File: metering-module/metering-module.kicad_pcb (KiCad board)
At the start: 2 copper layers, 87 x 31 mm, 25 parts, among them J1 North, J2 South, Q1 MMBT3904, Q2 MMBT3904, U1 LTV-817S, U2 LTV-817S, U3 BA033CC0FP-E2, U4 MAX3486, U5 MAX3486

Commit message: Ongoing
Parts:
- added J3: West, Connector_PinHeader_2.54mm:PinHeader_1x14_P2.54mm_Vertical, F.Cu at (163.5, 83.2)
- added J4: East, Connector_PinHeader_2.54mm:PinHeader_1x14_P2.54mm_Vertical, F.Cu at (130.3, 108.0)
- added J5: RJ12, Connector_RJ:RJ12_Amphenol_54601, F.Cu at (117.4, 84.0)
- moved C1 7.65 mm to (136.2, 101.6)
- moved C2 7.65 mm to (141.0, 101.6)
- moved D1 7.65 mm to (131.2, 88.1)
- moved D2 7.65 mm to (131.2, 91.6)
- moved F1 7.65 mm to (131.2, 99.1)
- moved R5 7.65 mm to (131.2, 95.1)
- moved U3 7.65 mm to (138.6, 92.9)
- moved R1 3.90 mm to (156.9, 89.5)
- moved U1 3.60 mm to (164.9, 89.2)

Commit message: Ongoing Work
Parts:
- removed H1, H2: MountingHole_Pad, MountingHole:MountingHole_4.3mm_M4
- removed J5: RJ12, Connector_RJ:RJ12_Amphenol_54601
- added C5: 100nF, Capacitor_SMD:C_1206_3216Metric_Pad1.33x1.80mm_HandSolder, F.Cu at (147.0, 97.5)
- added C6: 100nF, Capacitor_SMD:C_1206_3216Metric_Pad1.33x1.80mm_HandSolder, F.Cu at (147.0, 89.5)
- added D5: D_TVS, Diode_SMD:D_0603_1608Metric_Pad1.05x0.95mm_HandSolder, F.Cu at (112.0, 87.5)
- added D6: D_TVS, Diode_SMD:D_0603_1608Metric_Pad1.05x0.95mm_HandSolder, F.Cu at (112.0, 84.0)
- added D7: D_TVS, Diode_SMD:D_0603_1608Metric_Pad1.05x0.95mm_HandSolder, F.Cu at (164.0, 103.0)
- added D8: D_TVS, Diode_SMD:D_0603_1608Metric_Pad1.05x0.95mm_HandSolder, F.Cu at (164.0, 107.5)
- added R10: R, Resistor_SMD:R_1206_3216Metric_Pad1.30x1.75mm_HandSolder, F.Cu at (169.0, 103.0)
- added R11: R, Resistor_SMD:R_1206_3216Metric_Pad1.30x1.75mm_HandSolder, F.Cu at (169.0, 107.5)
- added R6: R, Resistor_SMD:R_1206_3216Metric_Pad1.30x1.75mm_HandSolder, F.Cu at (118.0, 87.5)
- added R7: R, Resistor_SMD:R_1206_3216Metric_Pad1.30x1.75mm_HandSolder, F.Cu at (118.0, 84.0)
- added R8: R, Resistor_SMD:R_1206_3216Metric_Pad1.30x1.75mm_HandSolder, F.Cu at (150.5, 97.5)
- added R9: R, Resistor_SMD:R_1206_3216Metric_Pad1.30x1.75mm_HandSolder, F.Cu at (150.5, 89.5)
- added TP1: Shield, TestPoint:TestPoint_Pad_D4.0mm, B.Cu at (143.0, 95.5)
- C2: value C -> 100nF
- R5: value R -> 10k
- moved J4 29.2 mm to (159.5, 108.5), turned to 270 degrees
- moved D4 17.8 mm to (175.5, 101.5)
- moved R4 8.35 mm to (171.0, 97.5), turned to 270 degrees
- moved D3 8.30 mm to (175.5, 85.0)
- moved U5 6.80 mm to (115.0, 92.5)
- moved C1 5.73 mm to (130.5, 101.0)
- moved U3 5.69 mm to (133.0, 92.0)
- moved C2 5.53 mm to (135.5, 101.0)
- moved D1 5.23 mm to (126.0, 87.5)
- moved D2 5.23 mm to (126.0, 91.0)
- moved F1 5.23 mm to (126.0, 98.5)
- moved R5 5.23 mm to (126.0, 94.5)
- moved C3 4.74 mm to (115.0, 97.5), turned to 0 degrees
- moved C4 4.74 mm to (115.0, 107.5), turned to 0 degrees
- moved J3 4.06 mm to (159.5, 82.5)
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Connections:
- J1 pad 5: Net-(J1-Pad5) -> Relay_1
- J1 pad 6: Net-(J1-Pad6) -> Relay_0
- J1 pad 7: Net-(J1-Pad7) -> GND1
- J1 pad 8: Net-(J1-Pad8) -> VS
- J2 pad 1: Net-(J2-Pad1) -> VCC
- J2 pad 2: Net-(J2-Pad2) -> GND
- J2 pad 5: Net-(J2-Pad5) -> RS485_0_A
- J2 pad 6: Net-(J2-Pad6) -> RS485_0_B
- J2 pad 7: Net-(J2-Pad7) -> RS485_1_A
- J2 pad 8: Net-(J2-Pad8) -> RS485_1_B
- U4 pad 6: RS485_0_A -> RS485_1_A
- U4 pad 7: RS485_0_B -> RS485_1_B
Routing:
- net +3V3: track 3.00 -> 71.6 mm
- net S0_1: track 0.00 -> 47.6 mm
- net VS: track 0.00 -> 43.1 mm
- net VCC: track 0.00 -> 36.3 mm
- net S0_0: track 0.00 -> 36.3 mm
- net GND1: track 0.00 -> 23.2 mm
- net GNDPWR: track 0.00 -> 21.9 mm
- net RS485_0_B: track 0.00 -> 15.0 mm
- net RS485_1_B: track 0.00 -> 12.7 mm
- net RS485_0_A: track 0.00 -> 12.5 mm
- net Relay_1: track 0.00 -> 11.3 mm
- net Relay_0: track 0.00 -> 10.3 mm
- net RS485_1_A: track 0.00 -> 9.93 mm
- net Net-(R4-Pad2): track 0.00 -> 3.85 mm
- net Net-(R3-Pad2): track 0.00 -> 3.85 mm
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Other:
- board size 87 x 31 mm -> 86 x 31 mm
- board text added: "BOT"
- board text added: "TOP"

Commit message: Ongoing Work. Still not ready for small and dedicated commits.
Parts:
- removed D5, D6: D_TVS, Diode_SMD:D_0603_1608Metric_Pad1.05x0.95mm_HandSolder
- removed R6, R7: R, Resistor_SMD:R_1206_3216Metric_Pad1.30x1.75mm_HandSolder
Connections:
- net Net-(J4-Pad4) renamed U0TXD
- net Net-(J4-Pad5) renamed U0RXD
- J1 pad 1: Net-(J1-Pad1) -> GND
- J1 pad 2: Net-(J1-Pad2) -> S0_1
- J1 pad 3: Net-(J1-Pad3) -> GND
- J1 pad 4: Net-(J1-Pad4) -> S0_0
- J2 pad 2: GND -> VCC
- J2 pad 3: Net-(J2-Pad3) -> GND
- J2 pad 4: Net-(J2-Pad4) -> GNDPWR
- J3 pad 10: Net-(J3-Pad10) -> RS485_0_TX
- J3 pad 12: Net-(J3-Pad12) -> S0_1
- J3 pad 13: Net-(J3-Pad13) -> SW0
- J3 pad 4: Net-(J3-Pad4) -> RS485_0_RX
- J3 pad 5: Net-(J3-Pad5) -> S0_0
- J3 pad 6: Net-(J3-Pad6) -> RS485_1_RX
- J3 pad 9: Net-(J3-Pad9) -> RS485_0_TXE
- J4 pad 10: Net-(J4-Pad10) -> SW1
- J4 pad 12: Net-(J4-Pad12) -> RS485_1_TXE
- J4 pad 13: Net-(J4-Pad13) -> RS485_1_TX
- U4 pad 1: RS485_0_RX -> RS485_1_RX
- U4 pad 2: RS485_0_TXE -> RS485_1_TXE
- U4 pad 3: RS485_0_TXE -> RS485_1_TXE
- U4 pad 4: RS485_0_TX -> RS485_1_TX
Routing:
- net GNDPWR: track 21.9 -> 95.3 mm
- net RS485_0_RX: track 0.00 -> 40.4 mm, vias 0 -> 1
- net RS485_1_RX: track 0.00 -> 38.5 mm, vias 0 -> 2
- net RS485_1_TXE: track 0.00 -> 27.0 mm
- net RS485_0_TXE: track 2.54 -> 27.0 mm, vias 0 -> 1
- net RS485_0_TX: track 0.00 -> 22.5 mm, vias 0 -> 1
- net RS485_1_TX: track 0.00 -> 16.6 mm
- net +3V3: track 71.6 -> 56.7 mm, vias 0 -> 2
- net S0_1: track 47.6 -> 61.8 mm
- net S0_0: track 36.3 -> 50.1 mm
- net Net-(D6-Pad2): track 3.58 -> 0.00 mm
- net Net-(D5-Pad2): track 3.58 -> 0.00 mm
- net VCC: track 36.3 -> 34.7 mm, vias 0 -> 1

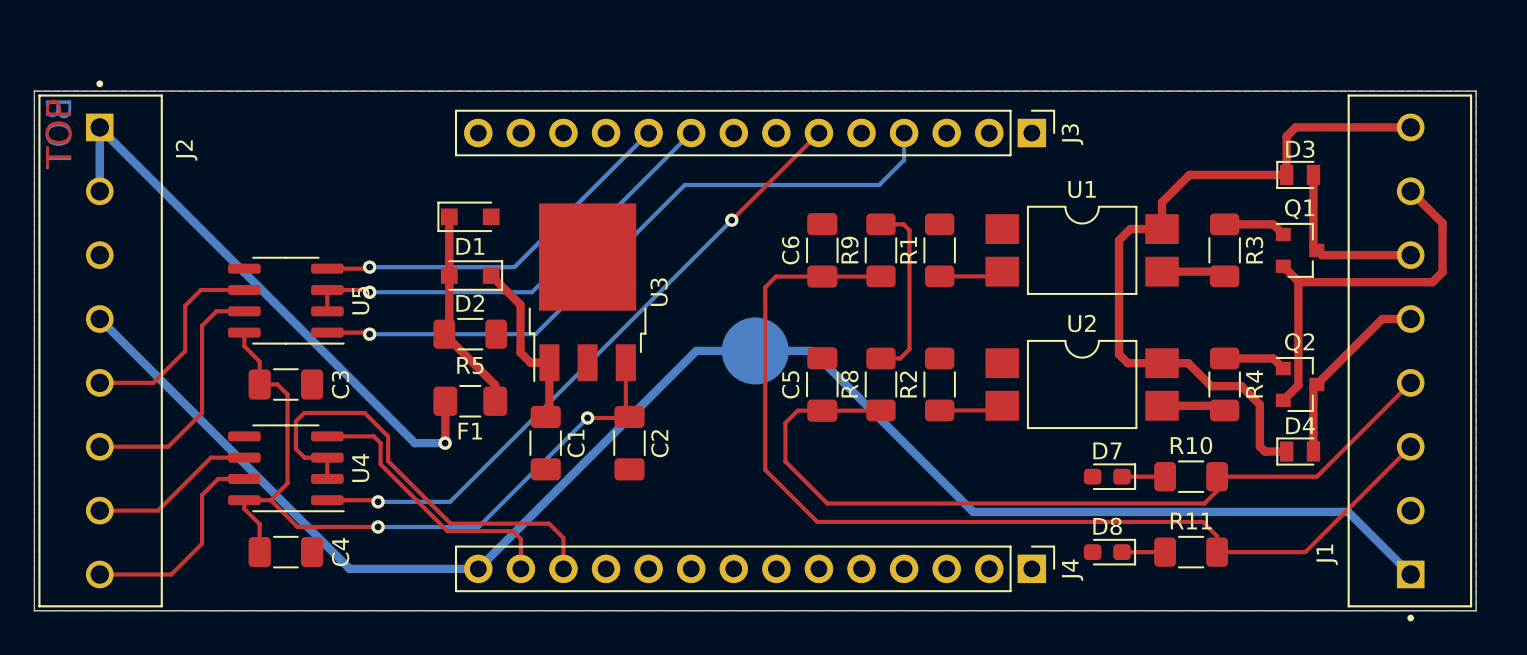
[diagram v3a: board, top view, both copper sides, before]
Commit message: Use a GPIO expander for metering module to safe pins
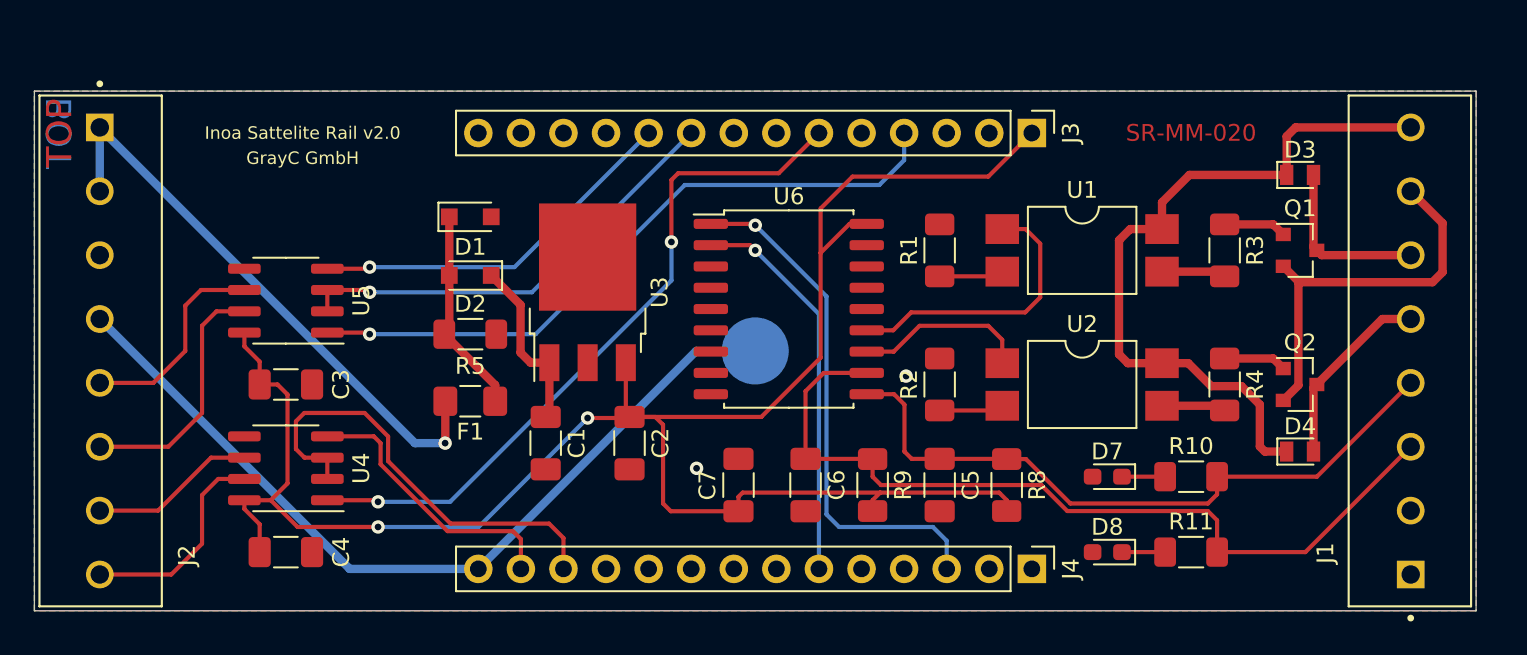
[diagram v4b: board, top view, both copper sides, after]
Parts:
- added C7: 100nF, Capacitor_SMD:C_1206_3216Metric_Pad1.33x1.80mm_HandSolder, F.Cu at (142.0, 103.5)
- added U6: MCP23008-xSO, Package_SO:SOIC-18W_7.5x11.6mm_P1.27mm, F.Cu at (145.0, 93.0)
- moved C6 14.0 mm to (146.0, 103.5), turned to 270 degrees
- moved R9 14.0 mm to (150.0, 103.5), turned to 270 degrees
- moved R8 9.60 mm to (158.0, 103.5), turned to 270 degrees
- moved C5 9.22 mm to (154.0, 103.5), turned to 270 degrees
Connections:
- net U0RXD renamed Net-(J4-Pad5)
- net U0TXD renamed Net-(J4-Pad4)
- J3 pad 12: S0_1 -> Net-(J3-Pad12)
- J3 pad 13: SW0 -> Net-(J3-Pad13)
- J3 pad 5: S0_0 -> Net-(J3-Pad5)
- J4 pad 10: SW1 -> Net-(J4-Pad10)
- J4 pad 3: Net-(J4-Pad3) -> I2C_SCL
- J4 pad 6: Net-(J4-Pad6) -> I2C_SDA
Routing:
- net +3V3: track 56.7 -> 115.8 mm
- net GNDPWR: track 95.3 -> 50.7 mm
- net I2C_SCL: track 0.00 -> 31.2 mm, vias 0 -> 1
- net I2C_SDA: track 0.00 -> 23.4 mm, vias 0 -> 1
- net SW0: track 0.00 -> 17.0 mm
- net S0_1: track 61.8 -> 50.9 mm
- net SW1: track 0.00 -> 10.5 mm
- net S0_0: track 50.1 -> 40.4 mm
- net RS485_1_RX: track 38.5 -> 42.0 mm
- net GND: vias 0 -> 2
- added copper zone on B.Cu, net GND
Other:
- board text added: "GrayC GmbH"
- board text added: "Inoa Sattelite Rail v2.0"
- board text added: "SR-MM-020"

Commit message: Introduce new serial numbering scheme
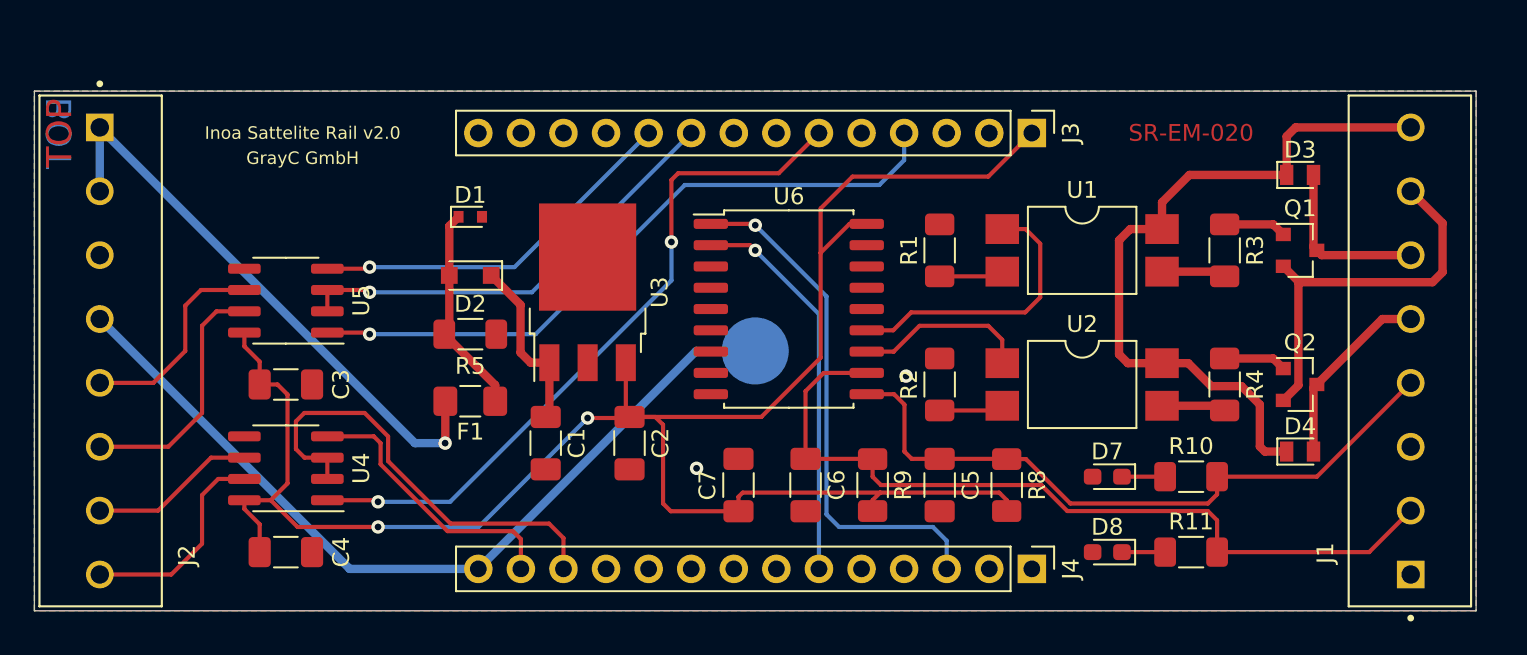
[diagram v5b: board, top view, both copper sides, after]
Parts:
- D1: value D_TVS -> 25V; footprint Diode_SMD:D_SOD-323_HandSoldering -> Diode_SMD:D_SOD-523
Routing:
- net S0_1: track 50.9 -> 49.3 mm
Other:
- board text added: "SR-EM-020"
- board text removed: "SR-MM-020"
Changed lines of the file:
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@@
     (thickness 1.6)
     (drawings 9)
-    (tracks 243)
+    (tracks 244)
     (zones 0)
     (modules 36)
@@
   )
   (setup
-    (last_trace_width 0.25)
+    (last_trace_width 0.5)
     (user_trace_width 0.5)
     (trace_clearance 0.2)
@@
     (add_net VS)
   )
+  (module Diode_SMD:D_SOD-523 (layer F.Cu)
+    (at 126 87.5)
+    (descr "http://www.diodes.com/datasheets/ap02001.pdf p.144")
+    (tags "Diode SOD523")
+    (attr smd)
+    (fp_text reference D1 (at 0 -1.3) (layer F.SilkS)
+      (effects (font (size 1 1) (thickness 0.15)))
+    )
+    (fp_text value 25V (at 0 1.4) (layer F.Fab)
+      (effects (font (size 1 1) (thickness 0.15)))
+    )
+    (fp_text user %R (at 0 -1.3) (layer F.Fab)
+      (effects (font (size 1 1) (thickness 0.15)))
+    )
+    (fp_line (start -1.15 -0.6) (end -1.15 0.6) (layer F.SilkS) (width 0.12))
+    (fp_line (start 1.25 -0.7) (end 1.25 0.7) (layer F.CrtYd) (width 0.05))
+    (fp_line (start -1.25 -0.7) (end 1.25 -0.7) (layer F.CrtYd) (width 0.05))
+    (fp_line (start -1.25 0.7) (end -1.25 -0.7) (layer F.CrtYd) (width 0.05))
+    (fp_line (start 1.25 0.7) (end -1.25 0.7) (layer F.CrtYd) (width 0.05))
+    (fp_line (start 0.1 0) (end 0.25 0) (layer F.Fab) (width 0.1))
+    (fp_line (start 0.1 -0.2) (end -0.2 0) (layer F.Fab) (width 0.1))
+    (fp_line (start 0.1 0.2) (end 0.1 -0.2) (layer F.Fab) (width 0.1))
+    (fp_line (start -0.2 0) (end 0.1 0.2) (layer F.Fab) (width 0.1))
+    (fp_line (start -0.2 0) (end -0.35 0) (layer F.Fab) (width 0.1))
+    (fp_line (start -0.2 0.2) (end -0.2 -0.2) (layer F.Fab) (width 0.1))
+    (fp_line (start 0.65 -0.45) (end 0.65 0.45) (layer F.Fab) (width 0.1))
+    (fp_line (start -0.65 -0.45) (end 0.65 -0.45) (layer F.Fab) (width 0.1))
+    (fp_line (start -0.65 0.45) (end -0.65 -0.45) (layer F.Fab) (width 0.1))
+    (fp_line (start 0.65 0.45) (end -0.65 0.45) (layer F.Fab) (width 0.1))
+    (fp_line (start 0.7 -0.6) (end -1.15 -0.6) (layer F.SilkS) (width 0.12))
+    (fp_line (start 0.7 0.6) (end -1.15 0.6) (layer F.SilkS) (width 0.12))
+    (pad 1 smd rect (at -0.7 0 180) (size 0.6 0.7) (layers F.Cu F.Paste F.Mask)
+      (net 4 "Net-(D1-Pad1)"))
+    (pad 2 smd rect (at 0.7 0 180) (size 0.6 0.7) (layers F.Cu F.Paste F.Mask)
+      (net 1 GND))
+    (model ${KISYS3DMOD}/Diode_SMD.3dshapes/D_SOD-523.wrl
+      (at (xyz 0 0 0))
+      (scale (xyz 1 1 1))
+      (rotate (xyz 0 0 0))
+    )
+  )
   (module Capacitor_SMD:C_1206_3216Metric_Pad1.33x1.80mm_HandSolder (layer F.Cu)
     (at 142 103.5 90)
@@
     (tags "test point SMD pad")
     (attr virtual)
-    (fp_text reference TP1 (at 0 2.898) (layer B.SilkS)
+    (fp_text reference TP1 (at 0 2.898) (layer B.SilkS) hide
       (effects (font (size 1 1) (thickness 0.15)) (justify mirror))
     )
-    (fp_text value Shield (at 0 -3.1) (layer B.Fab)
+    (fp_text value Shield (at 0 -3.1) (layer B.SilkS)
       (effects (font (size 1 1) (thickness 0.15)) (justify mirror))
     )
@@
     )
   )
-  (module Diode_SMD:D_SOD-323_HandSoldering (layer F.Cu)
-    (at 126 87.5)
-    (descr SOD-323)
-    (tags SOD-323)
-    (attr smd)
-    (fp_text reference D1 (at 0 1.8) (layer F.SilkS)
-      (effects (font (size 1 1) (thickness 0.15)))
-    )
-    (fp_text value D_TVS (at 0.1 1.9) (layer F.Fab)
-      (effects (font (size 1 1) (thickness 0.15)))
-    )
-    (fp_line (start -1.9 -0.85) (end -1.9 0.85) (layer F.SilkS) (width 0.12))
-    (fp_line (start 0.2 0) (end 0.45 0) (layer F.Fab) (width 0.1))
-    (fp_line (start 0.2 0.35) (end -0.3 0) (layer F.Fab) (width 0.1))
-    (fp_line (start 0.2 -0.35) (end 0.2 0.35) (layer F.Fab) (width 0.1))
-    (fp_line (start -0.3 0) (end 0.2 -0.35) (layer F.Fab) (width 0.1))
-    (fp_line (start -0.3 0) (end -0.5 0) (layer F.Fab) (width 0.1))
-    (fp_line (start -0.3 -0.35) (end -0.3 0.35) (layer F.Fab) (width 0.1))
-    (fp_line (start -0.9 0.7) (end -0.9 -0.7) (layer F.Fab) (width 0.1))
-    (fp_line (start 0.9 0.7) (end -0.9 0.7) (layer F.Fab) (width 0.1))
-    (fp_line (start 0.9 -0.7) (end 0.9 0.7) (layer F.Fab) (width 0.1))
-    (fp_line (start -0.9 -0.7) (end 0.9 -0.7) (layer F.Fab) (width 0.1))
-    (fp_line (start -2 -0.95) (end 2 -0.95) (layer F.CrtYd) (width 0.05))
-    (fp_line (start 2 -0.95) (end 2 0.95) (layer F.CrtYd) (width 0.05))
-    (fp_line (start -2 0.95) (end 2 0.95) (layer F.CrtYd) (width 0.05))
-    (fp_line (start -2 -0.95) (end -2 0.95) (layer F.CrtYd) (width 0.05))
-    (fp_line (start -1.9 0.85) (end 1.25 0.85) (layer F.SilkS) (width 0.12))
-    (fp_line (start -1.9 -0.85) (end 1.25 -0.85) (layer F.SilkS) (width 0.12))
-    (fp_text user %R (at 0 -1.85) (layer F.Fab)
-      (effects (font (size 1 1) (thickness 0.15)))
-    )
-    (pad 2 smd rect (at 1.25 0) (size 1 1) (layers F.Cu F.Paste F.Mask)
-      (net 1 GND))
-    (pad 1 smd rect (at -1.25 0) (size 1 1) (layers F.Cu F.Paste F.Mask)
-      (net 4 "Net-(D1-Pad1)"))
-    (model ${KISYS3DMOD}/Diode_SMD.3dshapes/D_SOD-323.wrl
-      (at (xyz 0 0 0))
-      (scale (xyz 1 1 1))
-      (rotate (xyz 0 0 0))
-    )
-  )
   (module Capacitor_SMD:C_1206_3216Metric_Pad1.33x1.80mm_HandSolder (layer F.Cu)
     (at 115 107.5)
@@
     (effects (font (size 0.75 0.75) (thickness 0.1)))
   )
-  (gr_text SR-MM-020 (at 169 82.5) (layer F.Cu)
+  (gr_text SR-EM-020 (at 169 82.5) (layer F.Cu)
     (effects (font (size 1 1) (thickness 0.15)))
   )
@@
   (via (at 139.5 102.5) (size 0.8) (drill 0.4) (layers F.Cu B.Cu) (net 1))
   (via (at 152 97) (size 0.8) (drill 0.4) (layers F.Cu B.Cu) (net 1))
-  (via (at 143 88) (size 0.8) (drill 0.4) (layers F.Cu B.Cu) (net 57))
-  (via (at 143 89.5) (size 0.8) (drill 0.4) (layers F.Cu B.Cu) (net 56))
   (segment (start 130.845 99.2925) (end 130.7 99.4375) (width 0.25) (layer F.Cu) (net 2))
   (segment (start 130.72 99.2175) (end 130.5 99.4375) (width 0.5) (layer F.Cu) (net 2))
@@
   (segment (start 148.8 85.1) (end 156.9 85.1) (width 0.25) (layer F.Cu) (net 3))
   (segment (start 124.45 94.2) (end 124.15 94.5) (width 0.25) (layer F.Cu) (net 4))
-  (segment (start 124.75 87.5) (end 124.75 91) (width 0.5) (layer F.Cu) (net 4))
   (segment (start 124.75 94.2) (end 124.45 94.5) (width 0.5) (layer F.Cu) (net 4))
   (segment (start 124.75 91) (end 124.75 94.2) (width 0.5) (layer F.Cu) (net 4))
   (segment (start 127.4875 97.5375) (end 124.45 94.5) (width 0.5) (layer F.Cu) (net 4))
   (segment (start 127.4875 98.5) (end 127.4875 97.5375) (width 0.5) (layer F.Cu) (net 4))
+  (segment (start 124.75 88.05) (end 125.3 87.5) (width 0.5) (layer F.Cu) (net 4))
+  (segment (start 124.75 91) (end 124.75 88.05) (width 0.5) (layer F.Cu) (net 4))
   (segment (start 176.3 89.3) (end 176.5 89.5) (width 0.5) (layer F.Cu) (net 5))
   (segment (start 176.3 85) (end 176.3 89.3) (width 0.5) (layer F.Cu) (net 5))
@@
   (segment (start 164.875 103) (end 167.45 103) (width 0.25) (layer F.Cu) (net 36))
   (segment (start 164.875 107.5) (end 167.45 107.5) (width 0.25) (layer F.Cu) (net 37))
-  (segment (start 175.815 107.5) (end 182.1 101.215) (width 0.25) (layer F.Cu) (net 38))
-  (segment (start 170.55 107.5) (end 175.815 107.5) (width 0.25) (layer F.Cu) (net 38))
   (segment (start 149.9875 101.9375) (end 150 101.95) (width 0.25) (layer F.Cu) (net 38))
   (segment (start 146 101.9375) (end 149.9875 101.9375) (width 0.25) (layer F.Cu) (net 38))
@@
   (segment (start 150 103) (end 150 101.95) (width 0.25) (layer F.Cu) (net 38))
   (segment (start 150.5 103.5) (end 150 103) (width 0.25) (layer F.Cu) (net 38))
+  (segment (start 179.625 107.5) (end 182.1 105.025) (width 0.25) (layer F.Cu) (net 38))
+  (segment (start 170.55 107.5) (end 179.625 107.5) (width 0.25) (layer F.Cu) (net 38))
   (segment (start 103.9 108.835) (end 108.165 108.835) (width 0.25) (layer F.Cu) (net 39))
   (segment (start 108.165 108.835) (end 110 107) (width 0.25) (layer F.Cu) (net 39))
@@
   (segment (start 131.56 106.66) (end 131.56 108.5) (width 0.25) (layer F.Cu) (net 43))
   (segment (start 130.70002 105.80002) (end 131.56 106.66) (width 0.25) (layer F.Cu) (net 43))
+  (via (at 143 89.5) (size 0.8) (drill 0.4) (layers F.Cu B.Cu) (net 56))
   (segment (start 142.69 89.19) (end 143 89.5) (width 0.25) (layer F.Cu) (net 56))
   (segment (start 140.35 89.19) (end 142.69 89.19) (width 0.25) (layer F.Cu) (net 56))
   (segment (start 146.8 93.3) (end 143 89.5) (width 0.25) (layer B.Cu) (net 56))
   (segment (start 146.8 108.5) (end 146.8 93.3) (width 0.25) (layer B.Cu) (net 56))
+  (via (at 143 88) (size 0.8) (drill 0.4) (layers F.Cu B.Cu) (net 57))
   (segment (start 142.92 87.92) (end 143 88) (width 0.25) (layer F.Cu) (net 57))
   (segment (start 140.35 87.92) (end 142.92 87.92) (width 0.25) (layer F.Cu) (net 57))
